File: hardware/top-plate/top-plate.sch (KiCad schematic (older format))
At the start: 47 parts

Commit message: Connect all PWM pins to LEDs; show PCB version number
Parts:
- removed HS4, HS5, HS6, HS7: HEATSINK, Mounting_Holes:MountingHole_2.2mm_M2, symbol HEATSINK
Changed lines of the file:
@@
-	1    0    0    -1
-$EndComp
-$Comp
-L HEATSINK HS5
-U 1 1 5829DC9C
-P 5800 6100
-F 0 "HS5" H 5927 6221 50  0000 L CNN
-F 1 "HEATSINK" H 5927 6130 50  0000 L CNN
-F 2 "Mounting_Holes:MountingHole_2.2mm_M2" H 5800 6100 50  0001 C CNN
-F 3 "" H 5800 6100 50  0000 C CNN
-	1    5800 6100
-	1    0    0    -1
-$EndComp
-$Comp
-L HEATSINK HS6
-U 1 1 5829DC9E
-P 6600 6100
-F 0 "HS6" H 6727 6221 50  0000 L CNN
-F 1 "HEATSINK" H 6727 6130 50  0000 L CNN
-F 2 "Mounting_Holes:MountingHole_2.2mm_M2" H 6600 6100 50  0001 C CNN
-F 3 "" H 6600 6100 50  0000 C CNN
-	1    6600 6100
-	1    0    0    -1
-$EndComp
-$Comp
-L HEATSINK HS7
-U 1 1 5829DCA0
-P 7400 6100
-F 0 "HS7" H 7527 6221 50  0000 L CNN
-F 1 "HEATSINK" H 7527 6130 50  0000 L CNN
-F 2 "Mounting_Holes:MountingHole_2.2mm_M2" H 7400 6100 50  0001 C CNN
-F 3 "" H 7400 6100 50  0000 C CNN
-	1    7400 6100
-	1    0    0    -1
-$EndComp
-$Comp
-L HEATSINK HS4
-U 1 1 5829DCA1
-P 8150 6100
-F 0 "HS4" H 8277 6221 50  0000 L CNN
-F 1 "HEATSINK" H 8277 6130 50  0000 L CNN
-F 2 "Mounting_Holes:MountingHole_2.2mm_M2" H 8150 6100 50  0001 C CNN
-F 3 "" H 8150 6100 50  0000 C CNN
-	1    8150 6100
 	1    0    0    -1
 $EndComp

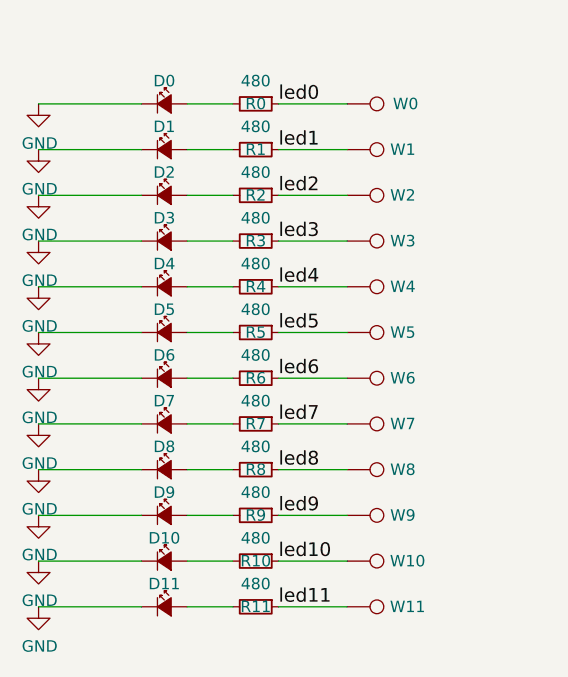
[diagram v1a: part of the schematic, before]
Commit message: Update version numbers on PCB silkscreens
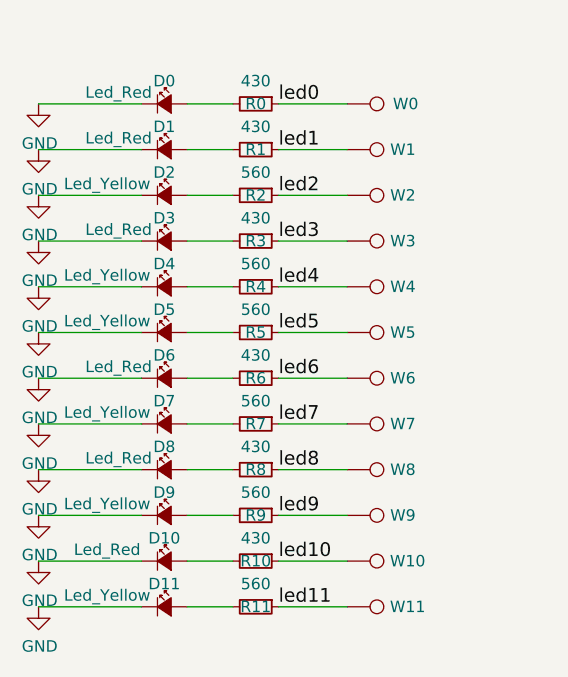
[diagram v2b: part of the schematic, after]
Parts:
- D0, D1, D10, D3, D6, D8: value Led_Small -> Led_Red
- D11, D2, D4, D5, D7, D9: value Led_Small -> Led_Yellow
- R0, R1, R10, R3, R6, R8: value 480 -> 430; footprint Resistors_SMD:R_1206_HandSoldering -> Resistors_SMD:R_1206
- R11, R2, R4, R5, R7, R9: value 480 -> 560; footprint Resistors_SMD:R_1206_HandSoldering -> Resistors_SMD:R_1206
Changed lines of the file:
@@
 Title "NaN-15"
 Date "2016-11-14"
-Rev "0.1"
+Rev "0.2"
 Comp ""
 Comment1 "Top plate"
@@
 P 4700 1700
 F 0 "D0" H 4700 1800 50  0000 C CNN
-F 1 "Led_Small" H 4700 1844 50  0001 C CNN
+F 1 "Led_Red" H 4500 1750 50  0000 C CNN
 F 2 "nan-15:LED_1206_REVERSE" V 4700 1700 50  0001 C CNN
 F 3 "" V 4700 1700 50  0000 C CNN
@@
 P 5100 1700
 F 0 "R0" V 5100 1700 50  0000 C CNN
-F 1 "480" V 5000 1700 50  0000 C CNN
-F 2 "Resistors_SMD:R_1206_HandSoldering" H 5100 1700 50  0001 C CNN
+F 1 "430" V 5000 1700 50  0000 C CNN
+F 2 "Resistors_SMD:R_1206" H 5100 1700 50  0001 C CNN
 F 3 "" H 5100 1700 50  0000 C CNN
 	1    5100 1700
@@
 P 4700 1900
 F 0 "D1" H 4700 2000 50  0000 C CNN
-F 1 "Led_Small" H 4700 2044 50  0001 C CNN
+F 1 "Led_Red" H 4500 1950 50  0000 C CNN
 F 2 "nan-15:LED_1206_REVERSE" V 4700 1900 50  0001 C CNN
 F 3 "" V 4700 1900 50  0000 C CNN
@@
 P 5100 1900
 F 0 "R1" V 5100 1900 50  0000 C CNN
-F 1 "480" V 5000 1900 50  0000 C CNN
-F 2 "Resistors_SMD:R_1206_HandSoldering" H 5100 1900 50  0001 C CNN
+F 1 "430" V 5000 1900 50  0000 C CNN
+F 2 "Resistors_SMD:R_1206" H 5100 1900 50  0001 C CNN
 F 3 "" H 5100 1900 50  0000 C CNN
 	1    5100 1900
@@
 P 4700 2100
 F 0 "D2" H 4700 2200 50  0000 C CNN
-F 1 "Led_Small" H 4700 2244 50  0001 C CNN
+F 1 "Led_Yellow" H 4450 2150 50  0000 C CNN
 F 2 "nan-15:LED_1206_REVERSE" V 4700 2100 50  0001 C CNN
 F 3 "" V 4700 2100 50  0000 C CNN
@@
 P 5100 2100
 F 0 "R2" V 5100 2100 50  0000 C CNN
-F 1 "480" V 5000 2100 50  0000 C CNN
-F 2 "Resistors_SMD:R_1206_HandSoldering" H 5100 2100 50  0001 C CNN
+F 1 "560" V 5000 2100 50  0000 C CNN
+F 2 "Resistors_SMD:R_1206" H 5100 2100 50  0001 C CNN
 F 3 "" H 5100 2100 50  0000 C CNN
 	1    5100 2100
@@
 P 4700 2300
 F 0 "D3" H 4700 2400 50  0000 C CNN
-F 1 "Led_Small" H 4700 2444 50  0001 C CNN
+F 1 "Led_Red" H 4500 2350 50  0000 C CNN
 F 2 "nan-15:LED_1206_REVERSE" V 4700 2300 50  0001 C CNN
 F 3 "" V 4700 2300 50  0000 C CNN
@@
 P 5100 2300
 F 0 "R3" V 5100 2300 50  0000 C CNN
-F 1 "480" V 5000 2300 50  0000 C CNN
-F 2 "Resistors_SMD:R_1206_HandSoldering" H 5100 2300 50  0001 C CNN
+F 1 "430" V 5000 2300 50  0000 C CNN
+F 2 "Resistors_SMD:R_1206" H 5100 2300 50  0001 C CNN
 F 3 "" H 5100 2300 50  0000 C CNN
 	1    5100 2300
@@
 P 4700 2500
 F 0 "D4" H 4700 2600 50  0000 C CNN
-F 1 "Led_Small" H 4700 2644 50  0001 C CNN
+F 1 "Led_Yellow" H 4450 2550 50  0000 C CNN
 F 2 "nan-15:LED_1206_REVERSE" V 4700 2500 50  0001 C CNN
 F 3 "" V 4700 2500 50  0000 C CNN
@@
 P 5100 2500
 F 0 "R4" V 5100 2500 50  0000 C CNN
-F 1 "480" V 5000 2500 50  0000 C CNN
-F 2 "Resistors_SMD:R_1206_HandSoldering" H 5100 2500 50  0001 C CNN
+F 1 "560" V 5000 2500 50  0000 C CNN
+F 2 "Resistors_SMD:R_1206" H 5100 2500 50  0001 C CNN
 F 3 "" H 5100 2500 50  0000 C CNN
 	1    5100 2500
@@
 P 4700 2700
 F 0 "D5" H 4700 2800 50  0000 C CNN
-F 1 "Led_Small" H 4700 2844 50  0001 C CNN
+F 1 "Led_Yellow" H 4450 2750 50  0000 C CNN
 F 2 "nan-15:LED_1206_REVERSE" V 4700 2700 50  0001 C CNN
 F 3 "" V 4700 2700 50  0000 C CNN
@@
 P 5100 2700
 F 0 "R5" V 5100 2700 50  0000 C CNN
-F 1 "480" V 5000 2700 50  0000 C CNN
-F 2 "Resistors_SMD:R_1206_HandSoldering" H 5100 2700 50  0001 C CNN
+F 1 "560" V 5000 2700 50  0000 C CNN
+F 2 "Resistors_SMD:R_1206" H 5100 2700 50  0001 C CNN
 F 3 "" H 5100 2700 50  0000 C CNN
 	1    5100 2700
@@
 P 4700 2900
 F 0 "D6" H 4700 3000 50  0000 C CNN
-F 1 "Led_Small" H 4700 3044 50  0001 C CNN
+F 1 "Led_Red" H 4500 2950 50  0000 C CNN
 F 2 "nan-15:LED_1206_REVERSE" V 4700 2900 50  0001 C CNN
 F 3 "" V 4700 2900 50  0000 C CNN
@@
 P 5100 2900
 F 0 "R6" V 5100 2900 50  0000 C CNN
-F 1 "480" V 5000 2900 50  0000 C CNN
-F 2 "Resistors_SMD:R_1206_HandSoldering" H 5100 2900 50  0001 C CNN
+F 1 "430" V 5000 2900 50  0000 C CNN
+F 2 "Resistors_SMD:R_1206" H 5100 2900 50  0001 C CNN
 F 3 "" H 5100 2900 50  0000 C CNN
 	1    5100 2900
@@
 P 4700 3100
 F 0 "D7" H 4700 3200 50  0000 C CNN
-F 1 "Led_Small" H 4700 3244 50  0001 C CNN
+F 1 "Led_Yellow" H 4450 3150 50  0000 C CNN
 F 2 "nan-15:LED_1206_REVERSE" V 4700 3100 50  0001 C CNN
 F 3 "" V 4700 3100 50  0000 C CNN
@@
 P 5100 3100
 F 0 "R7" V 5100 3100 50  0000 C CNN
-F 1 "480" V 5000 3100 50  0000 C CNN
-F 2 "Resistors_SMD:R_1206_HandSoldering" H 5100 3100 50  0001 C CNN
+F 1 "560" V 5000 3100 50  0000 C CNN
+F 2 "Resistors_SMD:R_1206" H 5100 3100 50  0001 C CNN
 F 3 "" H 5100 3100 50  0000 C CNN
 	1    5100 3100
@@
 P 4700 3300
 F 0 "D8" H 4700 3400 50  0000 C CNN
-F 1 "Led_Small" H 4700 3444 50  0001 C CNN
+F 1 "Led_Red" H 4500 3350 50  0000 C CNN
 F 2 "nan-15:LED_1206_REVERSE" V 4700 3300 50  0001 C CNN
 F 3 "" V 4700 3300 50  0000 C CNN
@@
 P 5100 3300
 F 0 "R8" V 5100 3300 50  0000 C CNN
-F 1 "480" V 5000 3300 50  0000 C CNN
-F 2 "Resistors_SMD:R_1206_HandSoldering" H 5100 3300 50  0001 C CNN
+F 1 "430" V 5000 3300 50  0000 C CNN
+F 2 "Resistors_SMD:R_1206" H 5100 3300 50  0001 C CNN
 F 3 "" H 5100 3300 50  0000 C CNN
 	1    5100 3300
@@
 P 4700 3500
 F 0 "D9" H 4700 3600 50  0000 C CNN
-F 1 "Led_Small" H 4700 3644 50  0001 C CNN
+F 1 "Led_Yellow" H 4450 3550 50  0000 C CNN
 F 2 "nan-15:LED_1206_REVERSE" V 4700 3500 50  0001 C CNN
 F 3 "" V 4700 3500 50  0000 C CNN
@@
 P 5100 3500
 F 0 "R9" V 5100 3500 50  0000 C CNN
-F 1 "480" V 5000 3500 50  0000 C CNN
-F 2 "Resistors_SMD:R_1206_HandSoldering" H 5100 3500 50  0001 C CNN
+F 1 "560" V 5000 3500 50  0000 C CNN
+F 2 "Resistors_SMD:R_1206" H 5100 3500 50  0001 C CNN
 F 3 "" H 5100 3500 50  0000 C CNN
 	1    5100 3500
@@
 P 4700 3700
 F 0 "D10" H 4700 3800 50  0000 C CNN
-F 1 "Led_Small" H 4700 3844 50  0001 C CNN
+F 1 "Led_Red" H 4450 3750 50  0000 C CNN
 F 2 "nan-15:LED_1206_REVERSE" V 4700 3700 50  0001 C CNN
 F 3 "" V 4700 3700 50  0000 C CNN
@@
 P 5100 3700
 F 0 "R10" V 5100 3700 50  0000 C CNN
-F 1 "480" V 5000 3700 50  0000 C CNN
-F 2 "Resistors_SMD:R_1206_HandSoldering" H 5100 3700 50  0001 C CNN
+F 1 "430" V 5000 3700 50  0000 C CNN
+F 2 "Resistors_SMD:R_1206" H 5100 3700 50  0001 C CNN
 F 3 "" H 5100 3700 50  0000 C CNN
 	1    5100 3700
@@
 P 4700 3900
 F 0 "D11" H 4700 4000 50  0000 C CNN
-F 1 "Led_Small" H 4700 4044 50  0001 C CNN
+F 1 "Led_Yellow" H 4450 3950 50  0000 C CNN
 F 2 "nan-15:LED_1206_REVERSE" V 4700 3900 50  0001 C CNN
 F 3 "" V 4700 3900 50  0000 C CNN
@@
 P 5100 3900
 F 0 "R11" V 5100 3900 50  0000 C CNN
-F 1 "480" V 5000 3900 50  0000 C CNN
-F 2 "Resistors_SMD:R_1206_HandSoldering" H 5100 3900 50  0001 C CNN
+F 1 "560" V 5000 3900 50  0000 C CNN
+F 2 "Resistors_SMD:R_1206" H 5100 3900 50  0001 C CNN
 F 3 "" H 5100 3900 50  0000 C CNN
 	1    5100 3900
